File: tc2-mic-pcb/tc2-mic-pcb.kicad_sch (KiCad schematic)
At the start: 14 parts, among them J401 Conn_02x03_Odd_Even, J402 Screw_Terminal_01x01, J403 Screw_Terminal_01x01, U401 AP7335-18SNG-7, U402 TXS0102DCT

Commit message: Add 2D barcode for microphone
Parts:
- added U403: (no value), cacophony-library:JLCPCB_QR_8mm, symbol cacophony-library:JLCPCB_QR_CODE
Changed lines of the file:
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@@
+	)
+	(symbol
+		(lib_id "cacophony-library:JLCPCB_QR_CODE")
+		(at 69.85 135.89 0)
+		(unit 1)
+		(body_style 1)
+		(exclude_from_sim yes)
+		(in_bom no)
+		(on_board yes)
+		(in_pos_files no)
+		(dnp no)
+		(fields_autoplaced yes)
+		(property "Reference" "U403"
+			(at 73.66 135.8899 0)
+			(show_name no)
+			(do_not_autoplace no)
+			(effects
+				(font
+					(size 1.27 1.27)
+				)
+				(justify left)
+			)
+		)
+		(property "Value" ""
+			(at 69.85 135.89 0)
+			(show_name no)
+			(do_not_autoplace no)
+			(effects
+				(font
+					(size 1.27 1.27)
+				)
+			)
+		)
+		(property "Footprint" "cacophony-library:JLCPCB_QR_8mm"
+			(at 69.85 135.89 0)
+			(hide yes)
+			(show_name no)
+			(do_not_autoplace no)
+			(effects
+				(font
+					(size 1.27 1.27)
+				)
+			)
+		)
+		(property "Datasheet" ""
+			(at 69.85 135.89 0)
+			(hide yes)
+			(show_name no)
+			(do_not_autoplace no)
+			(effects
+				(font
+					(size 1.27 1.27)
+				)
+			)
+		)
+		(property "Description" ""
+			(at 69.85 135.89 0)
+			(hide yes)
+			(show_name no)
+			(do_not_autoplace no)
+			(effects
+				(font
+					(size 1.27 1.27)
+				)
+			)
+		)
+		(instances
+			(project "tc2-mic-pcb"
+				(path "/5f96247b-0b73-48aa-a1a8-3d96ade9d103"
+					(reference "U403")
+					(unit 1)
+				)
+			)
+		)
 	)
 	(symbol

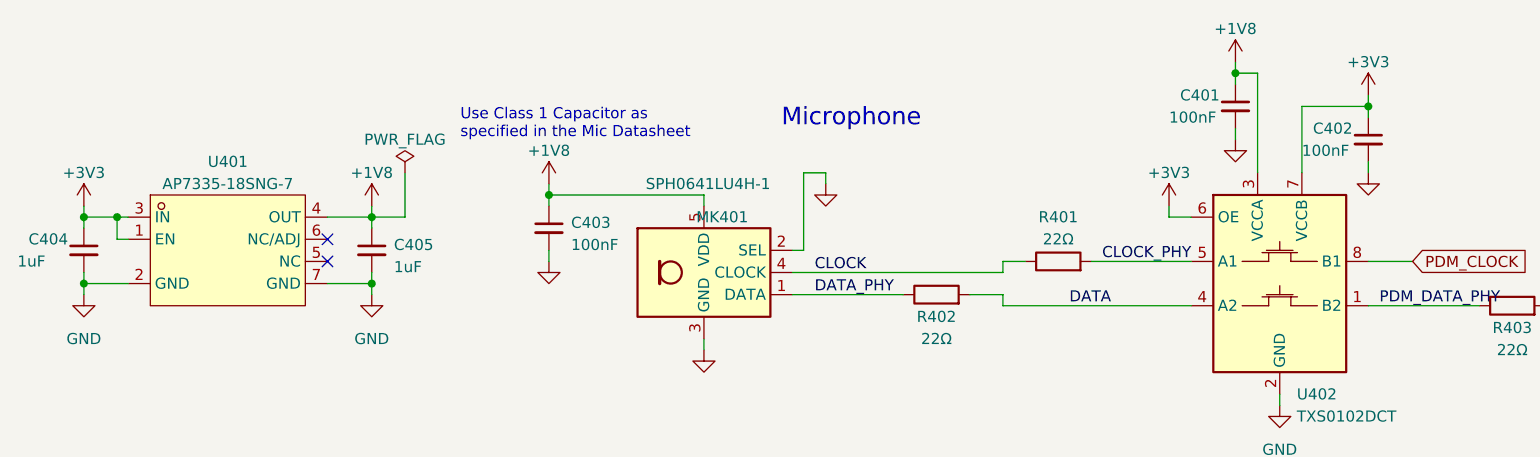
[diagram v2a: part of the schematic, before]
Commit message: Add git hash to PCBs
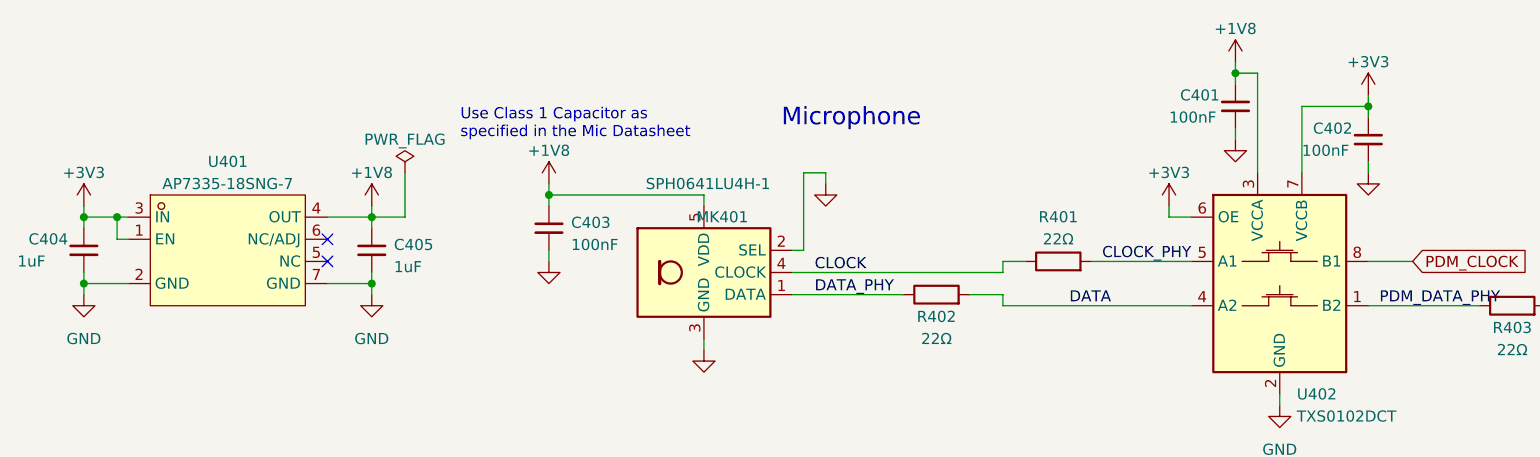
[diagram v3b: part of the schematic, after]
